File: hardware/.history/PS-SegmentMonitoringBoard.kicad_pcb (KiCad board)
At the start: 2 copper layers, 121 parts, among them IC1 BQ79616PAPR, J1 voltTapsConn, J2 highSideConn, J3 lowSideConn, J4 thermsConn, Q1 ZXTN4004KTC

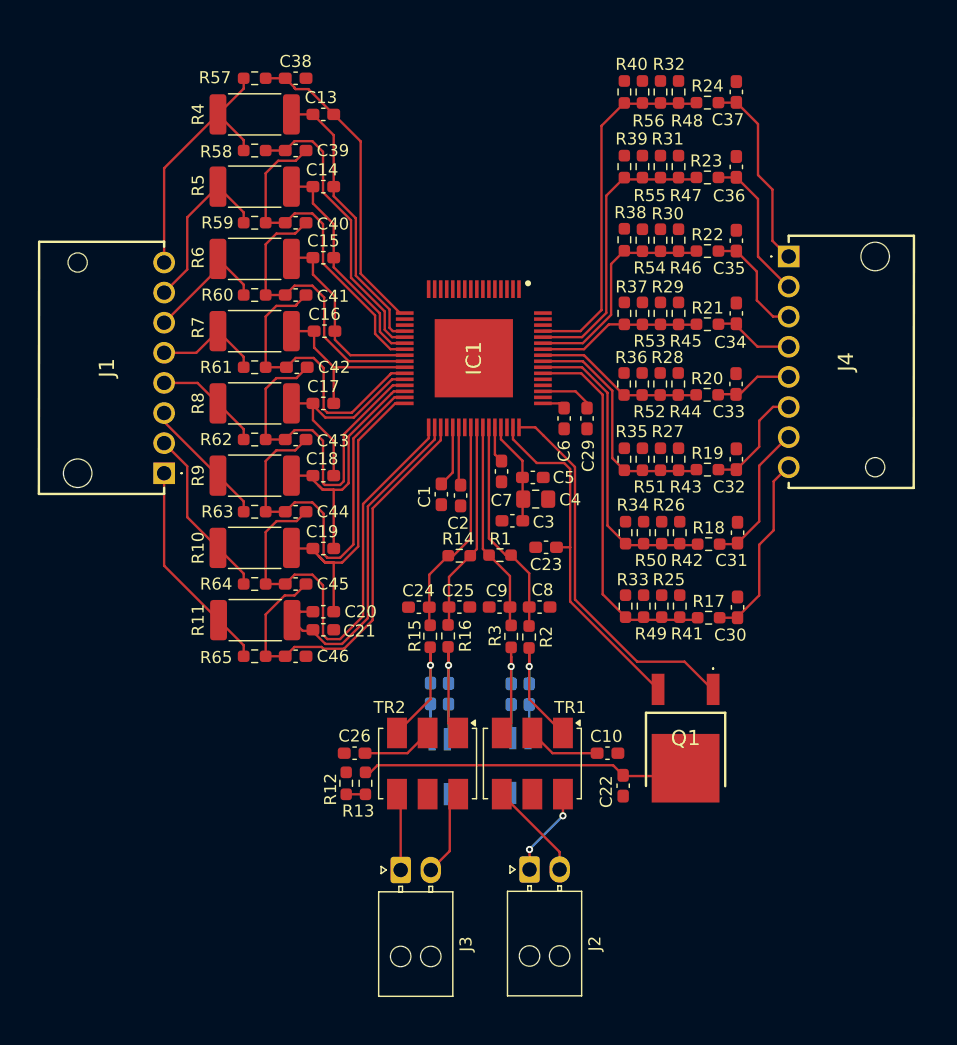
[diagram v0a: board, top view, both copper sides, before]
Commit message: 3rd schem review changes, layout v1
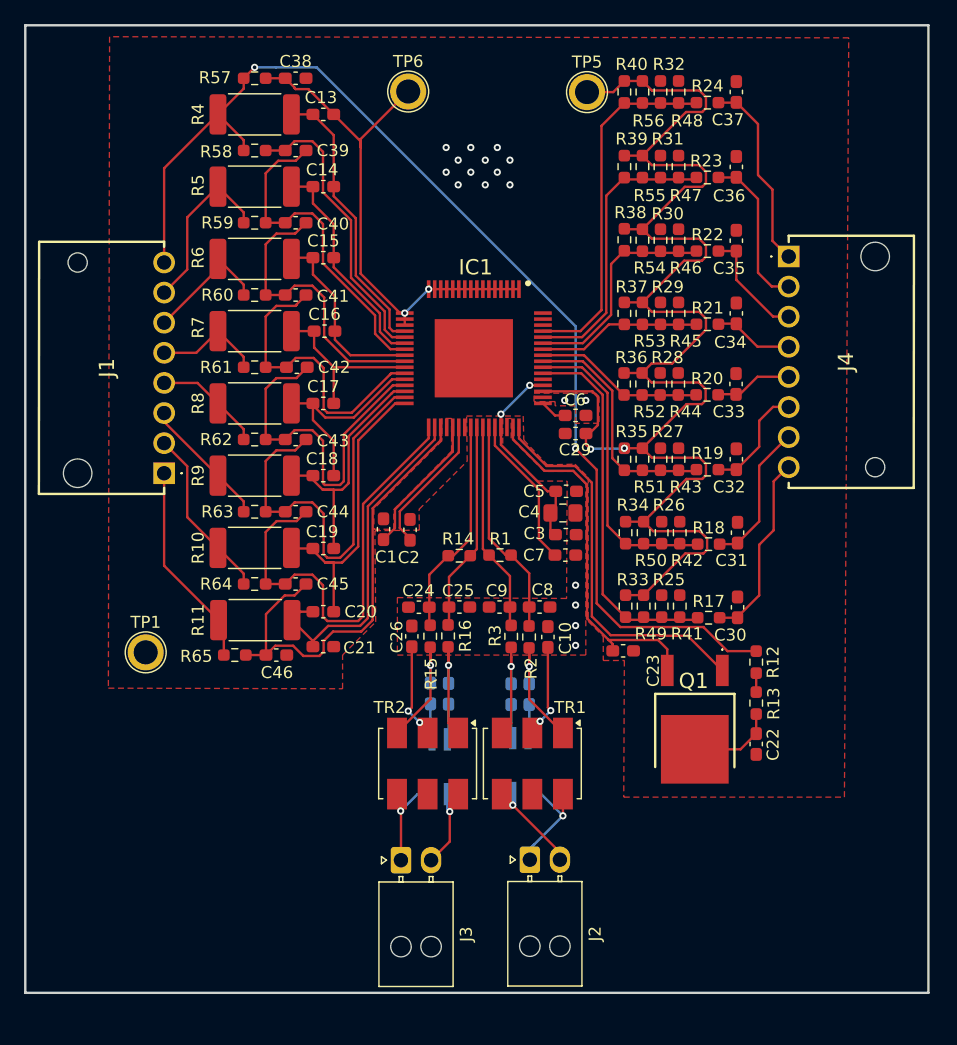
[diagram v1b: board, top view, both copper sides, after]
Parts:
- added TP1: AVSS, TestPoint:TestPoint_Plated_Hole_D2.0mm, F.Cu at (90.2, 112.9)
- added TP5: TSREF, TestPoint:TestPoint_Plated_Hole_D2.0mm, F.Cu at (126.9, 66.4)
- added TP6: BAT, TestPoint:TestPoint_Plated_Hole_D2.0mm, F.Cu at (112.0, 66.3)
- J1, J4: footprint Custom-Footprints:1053131308 -> LHRS_Connectors:Molex_Nano-Fit_105313-xx08_1x08_P2.50mm_Horizontal
- moved R12 35.5 mm to (140.9, 113.7)
- moved R13 33.1 mm to (140.9, 117.1), turned to -90 degrees
- moved C22 11.6 mm to (140.9, 120.5)
- moved C10 10.8 mm to (123.7, 111.7), turned to -90 degrees
- moved C26 10.8 mm to (112.3, 111.6), turned to -90 degrees
- moved C23 10.7 mm to (129.9, 112.8), turned to 0 degrees
- moved C7 8.74 mm to (125.1, 104.8), turned to 180 degrees
- moved C1 5.61 mm to (110.0, 102.7), turned to 90 degrees
- moved C2 5.08 mm to (112.2, 102.8), turned to 90 degrees
- moved C3 4.58 mm to (125.1, 103.2), turned to 0 degrees
- moved C5 2.99 mm to (125.2, 99.5)
- moved C4 2.54 mm to (124.9, 101.3)
- moved Q1 1.75 mm to (135.8, 118.5)
- moved R65 1.65 mm to (97.7, 113.2)
- moved C46 1.60 mm to (101.1, 113.2)
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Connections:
- C1 pad 2: AVSS -> REFHM
- C10 pad 1: AVSS -> CVSS
- C24 pad 2: AVSS -> CVSS
- C25 pad 2: AVSS -> CVSS
- C26 pad 1: AVSS -> CVSS
- C3 pad 2: AVSS -> CVSS
- C4 pad 2: AVSS -> CVSS
- C5 pad 2: AVSS -> CVSS
- C6 pad 2: AVSS -> DVSS
- C7 pad 1: AVSS -> CVSS
- C8 pad 2: AVSS -> CVSS
- C9 pad 2: AVSS -> CVSS
- IC1 pad 36: AVSS -> REFHM
- IC1 pad 46: AVSS -> CVSS
- IC1 pad 50: AVSS -> DVSS
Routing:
- net /TSREF: track 4.49 -> 123.5 mm, vias 0 -> 2
- net /Cell_Balancing/V7: track 23.6 -> 99.1 mm, vias 0 -> 2
- net Net-(Q1-C): track 28.5 -> 7.26 mm
- net /extraCells: track 26.1 -> 43.7 mm, vias 0 -> 2
- net Net-(IC1-NEG5V): track 3.03 -> 12.7 mm
- net /CVDD: track 8.37 -> 17.1 mm, vias 0 -> 2
- net Net-(IC1-AVDD): track 4.86 -> 11.8 mm
- net Net-(IC1-REFHP): track 5.09 -> 11.7 mm
- net /highSideIsolation/isolatedCOMHP: track 7.41 -> 10.9 mm, vias 2 -> 1
- net /Volt_Taps/VC0: track 36.5 -> 39.1 mm
- net /lowSideIsolation/isolatedCOMLP: track 6.43 -> 8.81 mm, vias 0 -> 1
- net Net-(C26-Pad2): track 5.89 -> 8.12 mm, vias 0 -> 2
- net /Volt_Taps/VC1: track 40.1 -> 38.0 mm
- net Net-(C10-Pad2): track 6.07 -> 7.87 mm, vias 0 -> 2
- net /LDOIN_NPN/LDOIN: track 29.2 -> 30.3 mm
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- added copper zone on F.Cu, net AVSS
- added copper zone on In1.Cu, net AVSS
- added copper zone on In2.Cu, net AVSS
- added copper zone on F.Cu, net CVSS
- added copper zone on In1.Cu, net CVSS
- added copper zone on F.Cu, net DVSS
- added copper zone on In1.Cu, net DVSS
- added copper zone on F.Cu, net REFHM
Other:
- board outline added: 75 x 80.3 mm
- copper layers 2 -> 4
- board text added: "Todo/Funky things I needa figure out: - CB routing/impedance matching - NTC impedance matching? - Via stitching? - # of/spacing of vias per GND pour connection?"

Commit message: layout fp updates, CB trace increases, n more
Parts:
- TR1, TR2: footprint RF_Mini-Circuits:Mini-Circuits_CD636_H4.11mm -> Custom-Footprints:SOP254P1270X685-6N
- moved J2 2.17 mm to (124.7, 132.3)
- moved J3 2.17 mm to (114.0, 132.3)
- moved TR2 0.54 mm to (113.1, 122.1)
- moved TR1 0.43 mm to (122.8, 122.2)
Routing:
- net /Cell_Balancing/V0: track 18.1 -> 35.2 mm
- net /Cell_Balancing/V6: track 14.5 -> 21.4 mm
- net /Cell_Balancing/V7: track 99.1 -> 105.5 mm
- net /lowSideIsolation/preIsolationCOMHN: track 10.5 -> 5.19 mm
- net /Cell_Balancing/V4: track 9.10 -> 14.4 mm
- net /lowSideIsolation/isolatedCOMLN: track 7.95 -> 13.1 mm, vias 1 -> 0
- net /Cell_Balancing/V5: track 11.0 -> 15.9 mm
- net /highSideIsolation/preIsolationCOMHN: track 9.67 -> 5.14 mm
- net /lowSideIsolation/isolatedCOMLP: track 8.81 -> 13.3 mm, vias 1 -> 0
- net /highSideIsolation/isolatedCOMHP: track 10.9 -> 15.1 mm, vias 1 -> 0
- net Net-(C26-Pad2): track 8.12 -> 4.19 mm
- net Net-(C10-Pad2): track 7.87 -> 4.00 mm, vias 2 -> 0
- net /highSideIsolation/preIsolationCOMHP: track 11.2 -> 7.61 mm, vias 1 -> 2
- net /highSideIsolation/isolatedCOMHN: track 8.67 -> 12.1 mm, vias 1 -> 2
- net /lowSideIsolation/preIsolationCOMHP: track 11.2 -> 8.00 mm
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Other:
- board size 75 x 80.3 mm -> 75 x 80.4 mm
